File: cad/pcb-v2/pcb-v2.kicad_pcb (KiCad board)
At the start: 2 copper layers, 19.6 x 17.6 mm, 2 parts, among them U1 ESP32-C3-MINI-1

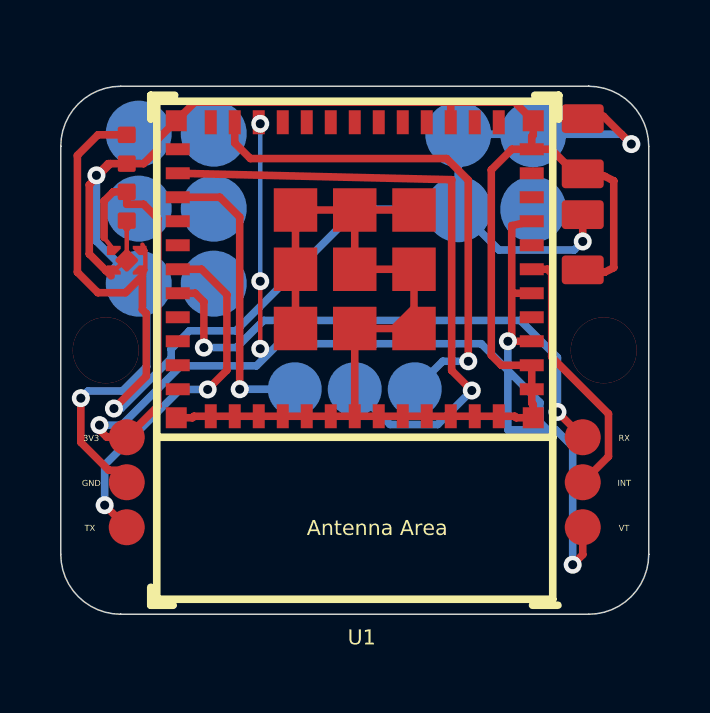
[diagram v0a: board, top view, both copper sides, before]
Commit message: Square the board, go diagonal on the screws, drop the stale Altium files
Outline -> 19.30 x 19.30 R2.0 (was 19.60 x 17.60). Gives up 0.30 in X to gain
1.70 in Y, which is the starved axis - U1's body is 16.6 of a 17.6 board.

Mounting holes -> O1.30 at (+8.10,-8.10) and (-8.10,+8.10), matching the v4
housing's M1.2 bosses. Diagonal, as asked. The other diagonal is impossible:
J4's pogo pad occupies the (-,-) corner and its position is set by the keyboard.
C3 +1.05 and C4 +1.20 in Y so the +X corner hole clears C4-1.

16 board-edge keepouts deleted - they were an artifact of the original Altium
import and Altium enforces edge clearance by design rule. The 2 antenna
keepouts are kept and extended to y=+9.30 into the new space.

12 segments ripped: 11 that terminated on the moved C3/C4 pads, plus one GND
return run left floating at both ends. Exactly 4 pads are now unrouted
(C3-1, C3-2, C4-1, C4-2) - for the autorouter. No orphan copper remains.

Deleted stale pcb-v2.PcbDoc / .PrjPcb / .PcbDoc.LOG. They predated every land
pattern fix and the handoff already marked them 'do not trust'.

Verified: parses clean, 95 pads, 175 tracks, 18 vias, 7 of 9 nets single-island,
one sub-0.127 pair (the known 0.1270 +3V3/VBAT one).
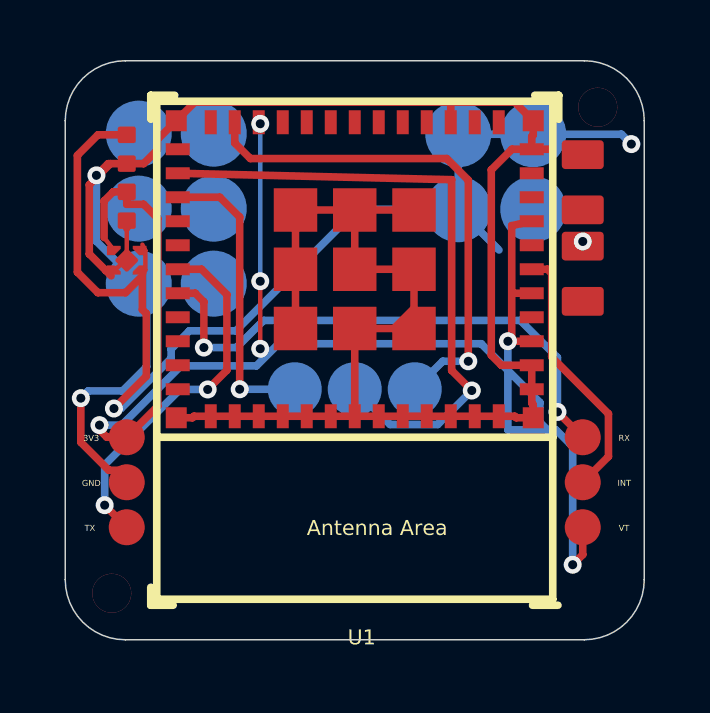
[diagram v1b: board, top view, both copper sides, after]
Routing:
- net GND: track 86.4 -> 79.9 mm
- net VBAT: track 45.1 -> 39.3 mm
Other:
- board size 19.6 x 17.6 mm -> 19.3 x 19.3 mm
